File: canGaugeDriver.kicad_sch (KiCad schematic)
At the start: 35 parts, among them J1 CANbed 1.0 Interface, J2 VIN INTERFACE, J3 348260240, J4 DB9'MEAL', U1 TPL7407LA, U2 TPL7407LA

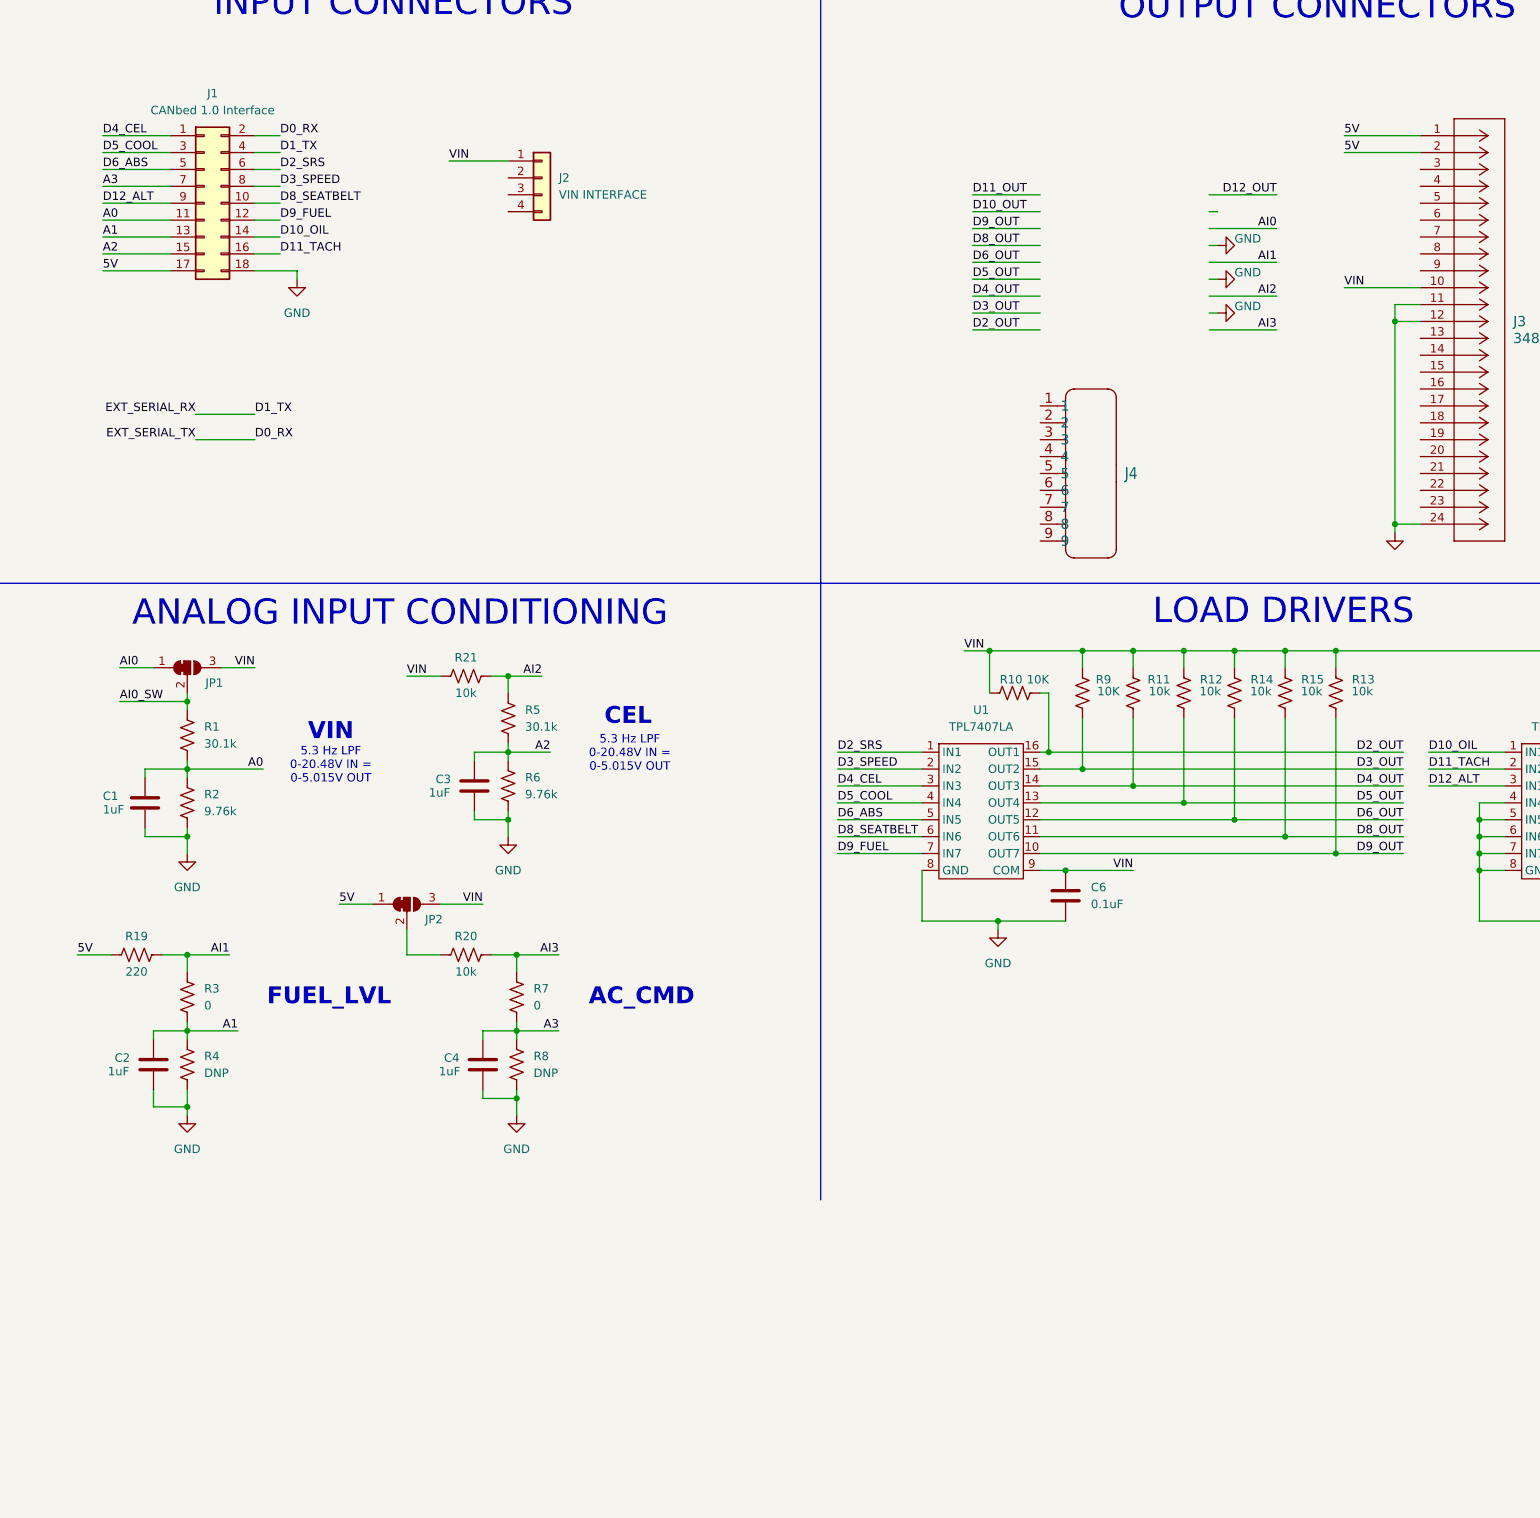
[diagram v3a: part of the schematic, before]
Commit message: added external connector pinout
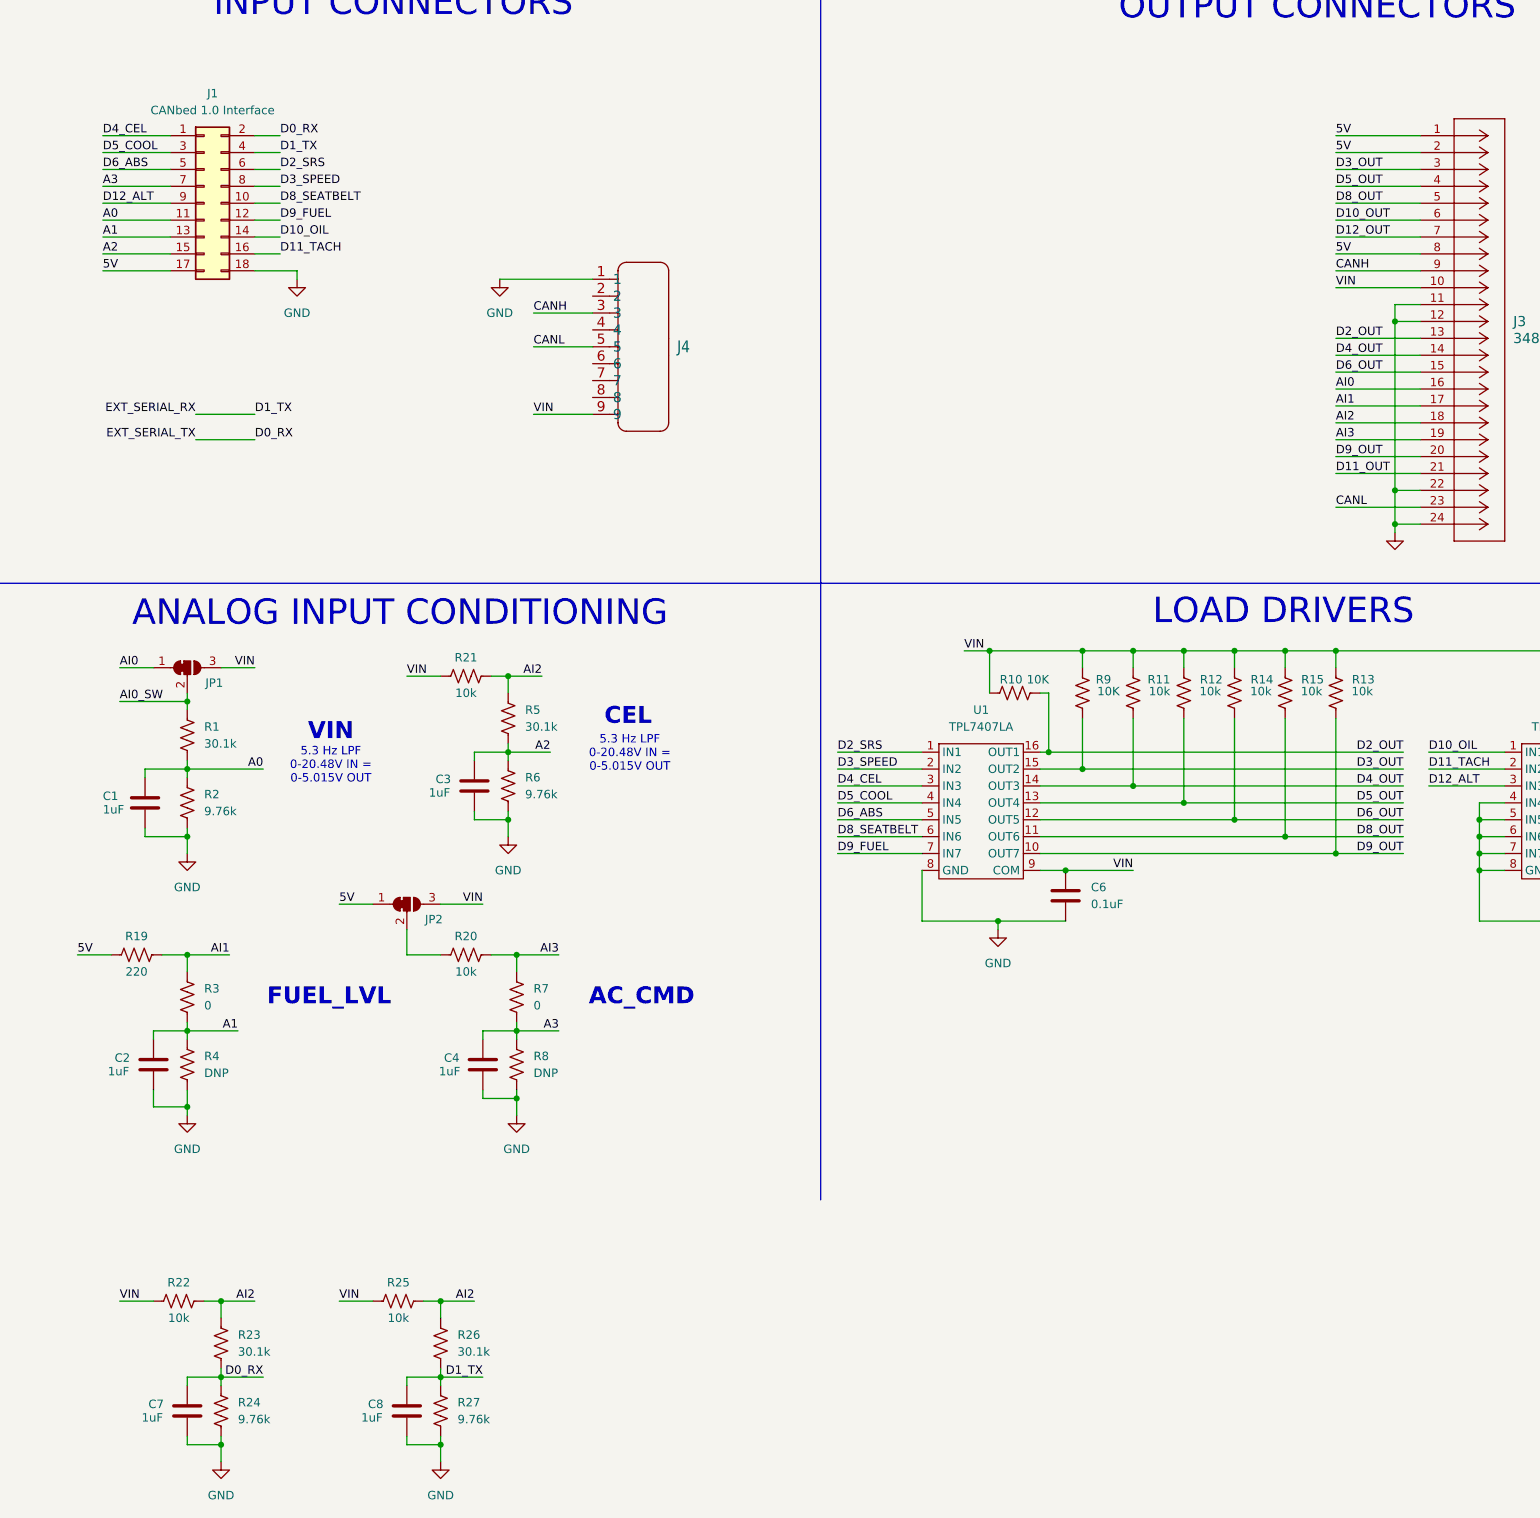
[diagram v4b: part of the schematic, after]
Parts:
- removed J2: VIN INTERFACE, canGaugeDriver:VIN_Pins, symbol Connector_Generic:Conn_01x04
- added C7, C8: 1uF, Capacitor_SMD:C_1206_3216Metric_Pad1.33x1.80mm_HandSolder, symbol Device:C
- added R22, R25: 10k, Resistor_SMD:R_0805_2012Metric_Pad1.20x1.40mm_HandSolder, symbol Device:R_US
- added R23, R26: 30.1k, Resistor_SMD:R_1206_3216Metric_Pad1.30x1.75mm_HandSolder, symbol Device:R_US
- added R24, R27: 9.76k, Resistor_SMD:R_1206_3216Metric_Pad1.30x1.75mm_HandSolder, symbol Device:R_US
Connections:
- net 5V: now also J3.8
- net AI0: now also J3.16
- net AI1: now also J3.17
- net AI2: now also J3.18, R22.1, R23.1, R25.1, R26.1
- net AI3: now also J3.19
- net D0_RX: now also C7.1, R23.2, R24.1
- net D10_OUT: now also J3.6
- net D11_OUT: now also J3.21
- net D12_OUT: now also J3.7
- net D1_TX: now also C8.1, R26.2, R27.1
- net D2_OUT: now also J3.13
- net D3_OUT: now also J3.3
- net D4_OUT: now also J3.14
- net D5_OUT: now also J3.4
- net D6_OUT: now also J3.15
- net D8_OUT: now also J3.5
- net D9_OUT: now also J3.20
- net GND: now also J3.22, J4.1, C7.2, C8.2, R24.2, R27.2
- net VIN: now also J4.9, R22.2, R25.2
- net CANH: now reaches J4.3
- net CANH: now also J3.9
- net CANL: now reaches J4.5
- net CANL: now also J3.23
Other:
- moved on the sheet: J4

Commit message: routed board
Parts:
- removed JP2: SolderJumper_3_Open, Jumper:SolderJumper-3_P1.3mm_Open_Pad1.0x1.5mm_NumberLabels, symbol Jumper:SolderJumper_3_Bridged12
- added JP2: SolderJumper_3_Open, Jumper:SolderJumper-3_P1.3mm_Open_Pad1.0x1.5mm_NumberLabels, symbol Jumper:SolderJumper_3_Open
- added R10, R11, R14, R2: 10k, Resistor_SMD:R_0805_2012Metric_Pad1.20x1.40mm_HandSolder, symbol Device:R_US
- C1, C2: footprint Capacitor_SMD:C_1206_3216Metric_Pad1.33x1.80mm_HandSolder -> Capacitor_SMD:C_0805_2012Metric_Pad1.18x1.45mm_HandSolder
- C3: renamed from C7; footprint Capacitor_SMD:C_1206_3216Metric_Pad1.33x1.80mm_HandSolder -> Capacitor_SMD:C_0805_2012Metric_Pad1.18x1.45mm_HandSolder
- C4: renamed from C3; footprint Capacitor_SMD:C_1206_3216Metric_Pad1.33x1.80mm_HandSolder -> Capacitor_SMD:C_0805_2012Metric_Pad1.18x1.45mm_HandSolder
- C5: renamed from C4; footprint Capacitor_SMD:C_1206_3216Metric_Pad1.33x1.80mm_HandSolder -> Capacitor_SMD:C_0805_2012Metric_Pad1.18x1.45mm_HandSolder
- C6: renamed from C8; footprint Capacitor_SMD:C_1206_3216Metric_Pad1.33x1.80mm_HandSolder -> Capacitor_SMD:C_0805_2012Metric_Pad1.18x1.45mm_HandSolder
- C7: renamed from C6; footprint Capacitor_SMD:C_1206_3216Metric_Pad1.33x1.80mm_HandSolder -> Capacitor_SMD:C_0805_2012Metric_Pad1.18x1.45mm_HandSolder
- C8: renamed from C5; footprint Capacitor_SMD:C_1206_3216Metric_Pad1.33x1.80mm_HandSolder -> Capacitor_SMD:C_0805_2012Metric_Pad1.18x1.45mm_HandSolder
- JP1: symbol Jumper:SolderJumper_3_Bridged12 -> Jumper:SolderJumper_3_Open
- R16: renamed from R5; footprint Resistor_SMD:R_1206_3216Metric_Pad1.30x1.75mm_HandSolder -> Resistor_SMD:R_0805_2012Metric_Pad1.20x1.40mm_HandSolder
- R17: renamed from R6; footprint Resistor_SMD:R_1206_3216Metric_Pad1.30x1.75mm_HandSolder -> Resistor_SMD:R_0805_2012Metric_Pad1.20x1.40mm_HandSolder
- R18: renamed from R7; footprint Resistor_SMD:R_1206_3216Metric_Pad1.30x1.75mm_HandSolder -> Resistor_SMD:R_0805_2012Metric_Pad1.20x1.40mm_HandSolder
- R19: renamed from R8; footprint Resistor_SMD:R_1206_3216Metric_Pad1.30x1.75mm_HandSolder -> Resistor_SMD:R_0805_2012Metric_Pad1.20x1.40mm_HandSolder
- R20: renamed from R26; footprint Resistor_SMD:R_1206_3216Metric_Pad1.30x1.75mm_HandSolder -> Resistor_SMD:R_0805_2012Metric_Pad1.20x1.40mm_HandSolder
- R21: renamed from R27; footprint Resistor_SMD:R_1206_3216Metric_Pad1.30x1.75mm_HandSolder -> Resistor_SMD:R_0805_2012Metric_Pad1.20x1.40mm_HandSolder
- R4: renamed from R1; footprint Resistor_SMD:R_1206_3216Metric_Pad1.30x1.75mm_HandSolder -> Resistor_SMD:R_0805_2012Metric_Pad1.20x1.40mm_HandSolder
- R5: renamed from R2; footprint Resistor_SMD:R_1206_3216Metric_Pad1.30x1.75mm_HandSolder -> Resistor_SMD:R_0805_2012Metric_Pad1.20x1.40mm_HandSolder
- R6: renamed from R3; footprint Resistor_SMD:R_1206_3216Metric_Pad1.30x1.75mm_HandSolder -> Resistor_SMD:R_0805_2012Metric_Pad1.20x1.40mm_HandSolder
- R7: renamed from R4; footprint Resistor_SMD:R_1206_3216Metric_Pad1.30x1.75mm_HandSolder -> Resistor_SMD:R_0805_2012Metric_Pad1.20x1.40mm_HandSolder
- R8: renamed from R23; value 30.1k -> 0; footprint Resistor_SMD:R_1206_3216Metric_Pad1.30x1.75mm_HandSolder -> Resistor_SMD:R_0805_2012Metric_Pad1.20x1.40mm_HandSolder
- R9: renamed from R24; value 9.76k -> DNP; footprint Resistor_SMD:R_1206_3216Metric_Pad1.30x1.75mm_HandSolder -> Resistor_SMD:R_0805_2012Metric_Pad1.20x1.40mm_HandSolder
- renumbered J4 to DB1, J3 to J2, R19 to R1, R20 to R12, R21 to R13, R25 to R15, R10 to R22, R9 to R23, R11 to R24, R12 to R25, R14 to R26, R15 to R27, R13 to R28, R16 to R29, R22 to R3, R17 to R30, R18 to R31
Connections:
- net 5V: now also R15.2, R3.2, JP2.1 (A), R10.2, R11.2; no longer J2.8, R1.2
- net AI2: now also R10.1; no longer R15.1, R20.1, R3.1, R8.1
- net AI3: now also R11.1
- net D10_OUT: now also J2.7; no longer J2.6
- net D11_OUT: now also J2.22; no longer J2.21
- net D12_OUT: now also J2.8; no longer J2.7
- net D2_OUT: now also J2.14, R22.1; no longer J2.13, R22.2
- net D3_OUT: now also J2.4; no longer J2.3
- net D4_OUT: now also J2.15; no longer J2.14
- net D5_OUT: now also J2.5; no longer J2.4
- net D6_OUT: now also J2.20; no longer J2.15
- net D8_OUT: now also J2.6; no longer J2.5
- net D9_OUT: now also J2.21; no longer J2.20
- net GND: no longer J2.22
- net VIN: now also R12.2, R22.2, JP2.3 (B), R14.2, R2.2; no longer R15.2, R22.1, R3.2
- new net: JP2.2 (C), R1.2
- new net D0_IN: J2.13, R2.1, R3.1, R8.1
- new net D1_IN: J2.3, R14.1, R15.1, R20.1
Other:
- note added: "A0 VIN"
- note added: "A1 FUEL_LVL"
- note added: "A2"
- note added: "A3"
- note added: "D0 AC_REQ"
- note added: "D1 CEL"
- note added: "INPUT CONDITIONING"
- note removed: "AC_CMD"
- note removed: "ANALOG INPUT CONDITIONING"
- note removed: "CEL"
- note removed: "FUEL_LVL"
- note removed: "VIN"
- moved on the sheet: C1, C2, C3, C4, C5, C6, C7, C8, J2, R1, R12, R13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

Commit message: more routing
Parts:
- added H1, H2, H3, H4: MountingHole, MountingHole:MountingHole_3mm, symbol Mechanical:MountingHole

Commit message: minor cleanup
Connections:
- net AI0 renamed A0_IN
- net AI1 renamed A1_IN
- net AI2 renamed A2_IN
- net AI3 renamed A3_IN
- net D0_RX renamed D0
- net D10_OIL renamed D10
- net D11_TACH renamed D11
- net D12_ALT renamed D12
- net D1_TX renamed D1
- net D2_SRS renamed D2
- net D3_SPEED renamed D3
- net D4_CEL renamed D4
- net D5_COOL renamed D5
- net D6_ABS renamed D6
- net D8_SEATBELT renamed D8
- net D9_FUEL renamed D9
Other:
- note added: "CEL COOLANT ABS ALTERNATOR"
- note added: "RX TX SRS SPEEDO SEATBELT FUEL OIL TACH"
- moved on the sheet: C7, R10, U1
